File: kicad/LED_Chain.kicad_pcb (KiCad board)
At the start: 2 copper layers, 63.6 x 31.5 mm, 34 parts, among them J1 Interface, J2 PWR, J3 NeoPixel R1 A, J4 NeoPixel R1 B, J5 NeoPixel R1 C, J6 NeoPixel R1 D, J7 LED, Q1 IRLML2502, Q2 IRLML2502, Q3 IRLML2502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

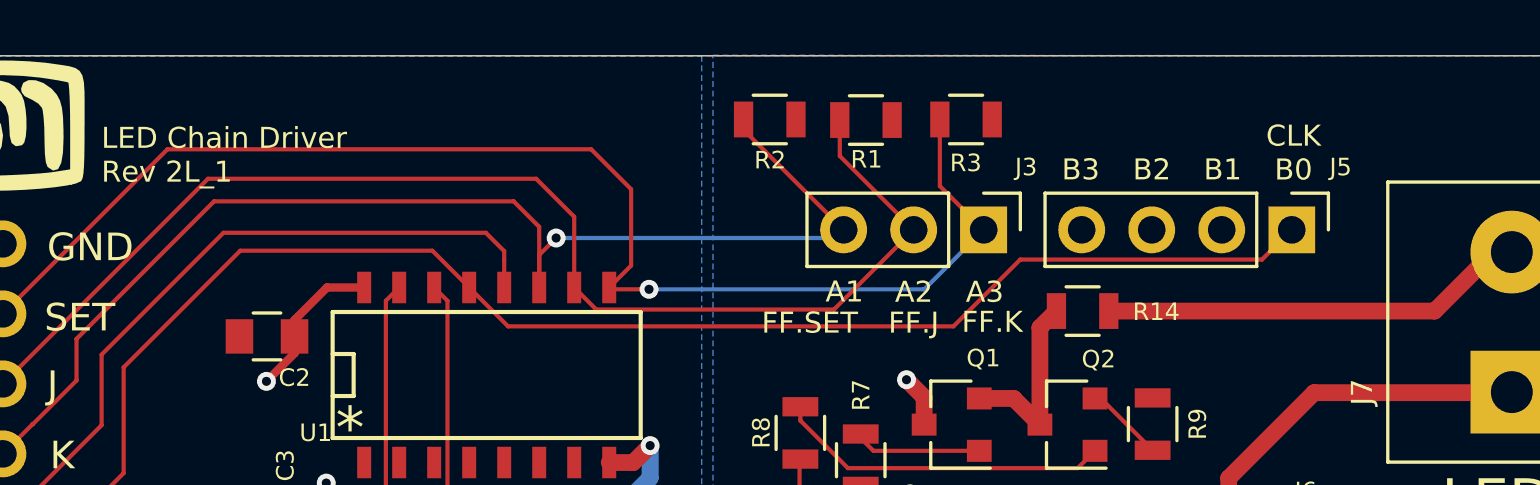
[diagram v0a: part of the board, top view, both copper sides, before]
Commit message: Revert "Fixes the pin association on J3"
This reverts commit 2cc36517f423e818af2cf15adf9433c164440afc.
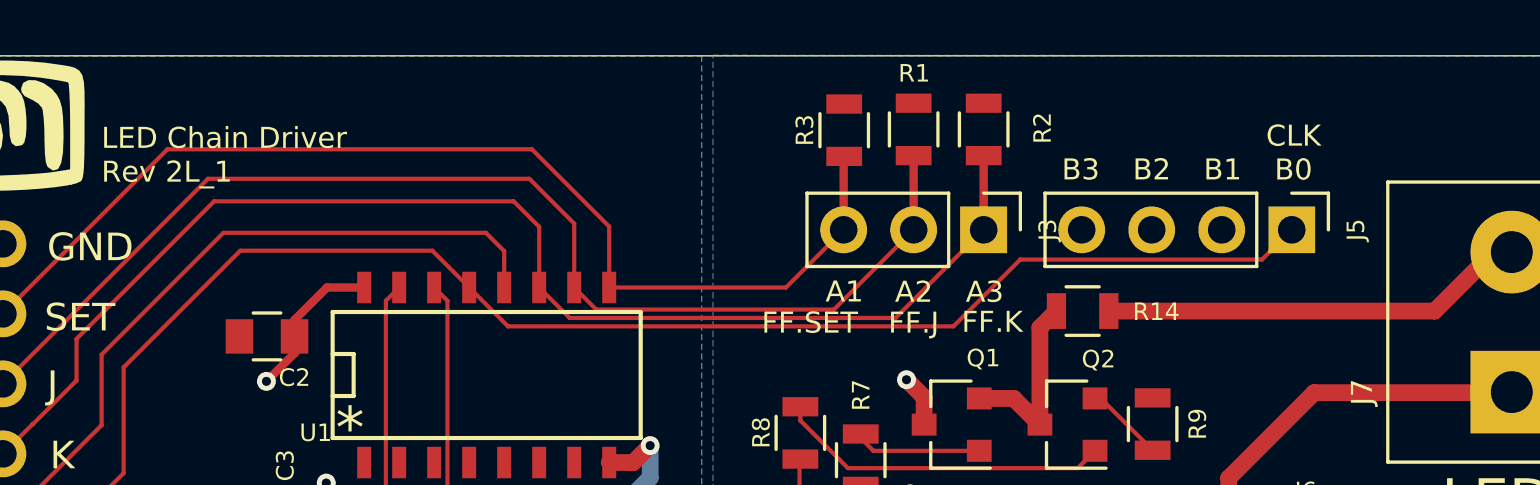
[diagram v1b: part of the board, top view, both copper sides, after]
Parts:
- moved R2 7.77 mm to (156.2, 82.6), turned to 90 degrees
- moved R3 4.44 mm to (151.2, 82.6), turned to 90 degrees
- moved R1 1.76 mm to (153.7, 82.6), turned to 90 degrees
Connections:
- J3 pad 1: /A1 -> /A3
- J3 pad 3: /A3 -> /A1
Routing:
- net /A1: track 49.0 -> 39.9 mm, vias 1 -> 0
- net /A2: track 45.9 -> 43.3 mm
- net /A3: track 44.8 -> 47.3 mm, vias 1 -> 0

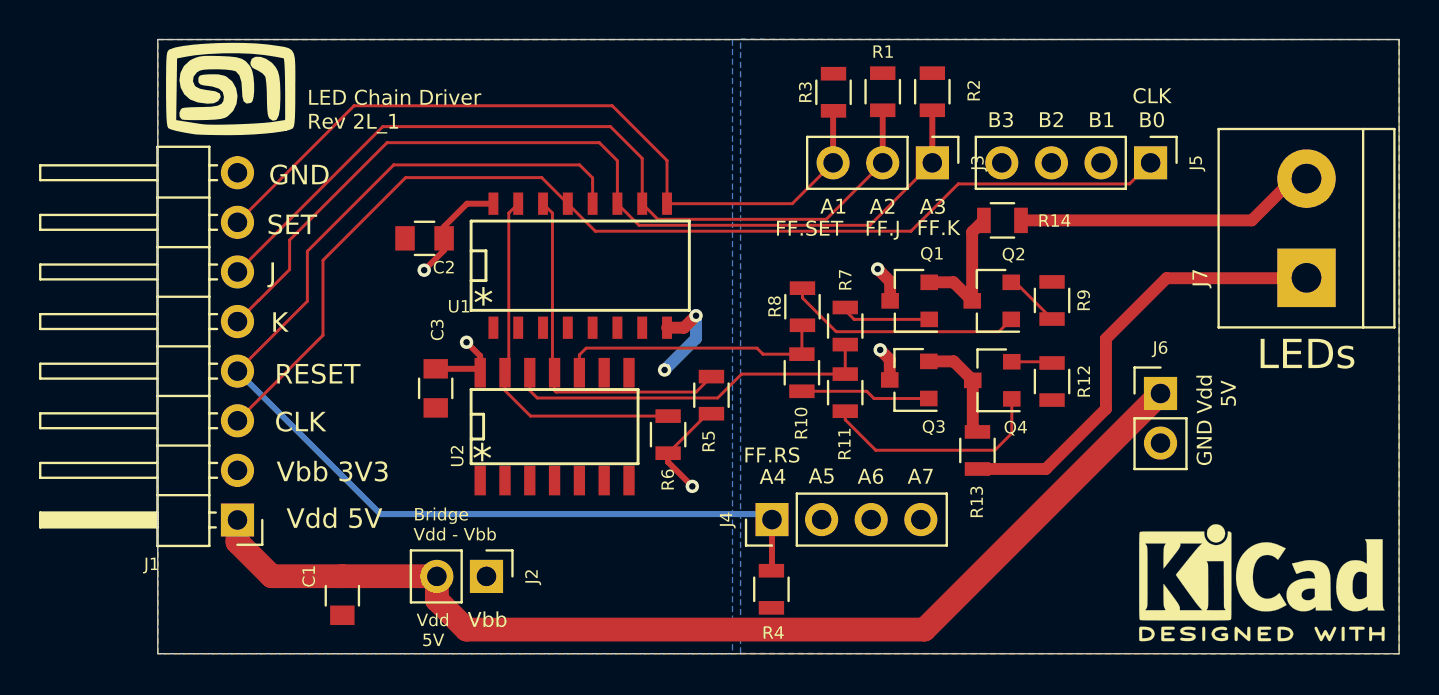
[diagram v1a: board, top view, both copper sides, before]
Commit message: Upgraded basic symbols and footprints
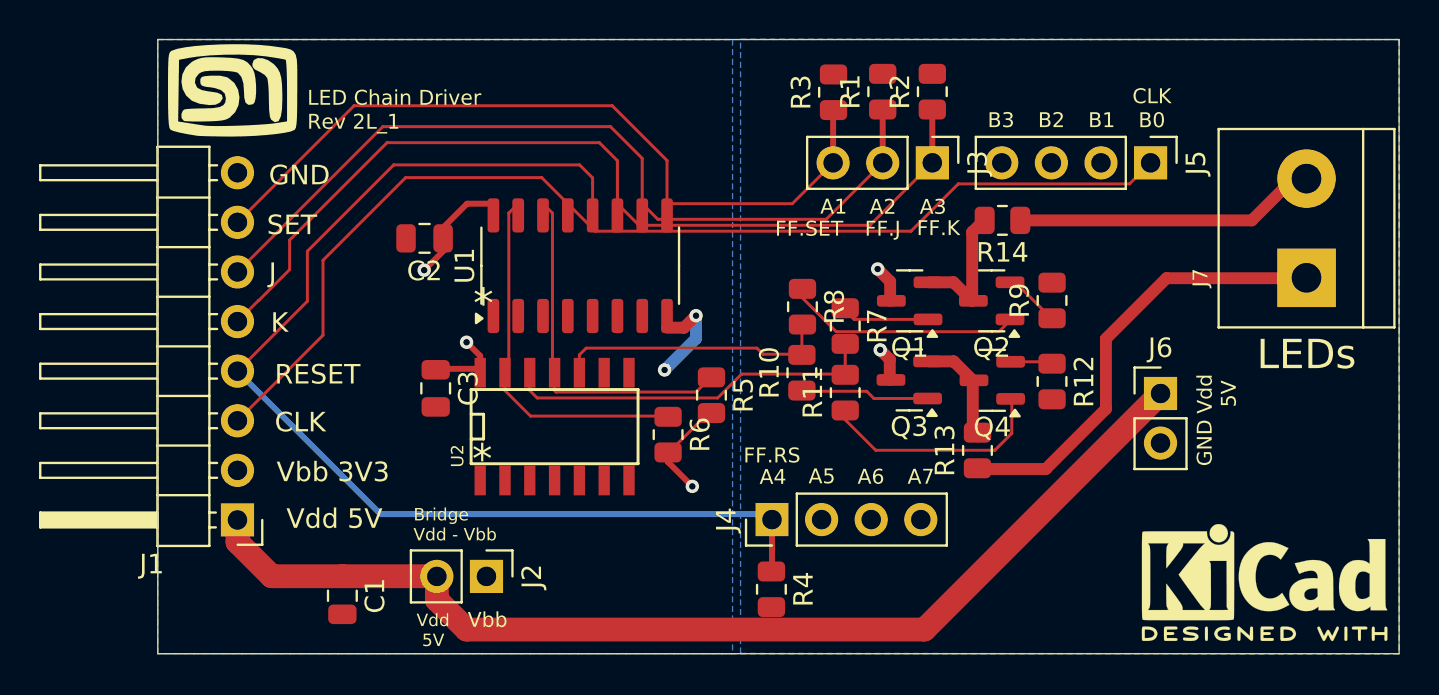
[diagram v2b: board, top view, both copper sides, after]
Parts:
- removed G*** (x2): LOGO, LED_Chain:MyBasic_rounded_50_1
- removed REF*** (x2): KiCad-Logo2_6mm_SilkScreen, Symbols:KiCad-Logo2_6mm_SilkScreen
- added Lg1: SM Logo, sjm-mechanical:MyBasic_rounded_50_1, F.Cu at (120.3, 82.5)
- added Lg2: KiCad Logo, Symbol:KiCad-Logo2_5mm_SilkScreen, F.Cu at (173.2, 107.7)
- added Lg3: SM Logo, sjm-mechanical:MyBasic_rounded_50_1, B.Cu at (149.7, 94.6)
- C1, C2, C3: footprint Capacitors_SMD:C_0805 -> Capacitor_SMD:C_0805_2012Metric
- J1: footprint Pin_Headers:Pin_Header_Angled_1x08_Pitch2.54mm -> Connector_PinHeader_2.54mm:PinHeader_1x08_P2.54mm_Horizontal
- J2, J6: footprint Pin_Headers:Pin_Header_Straight_1x02_Pitch2.54mm -> Connector_PinHeader_2.54mm:PinHeader_1x02_P2.54mm_Vertical
- J3: footprint Pin_Headers:Pin_Header_Straight_1x03_Pitch2.54mm -> Connector_PinHeader_2.54mm:PinHeader_1x03_P2.54mm_Vertical
- J4, J5: footprint Pin_Headers:Pin_Header_Straight_1x04_Pitch2.54mm -> Connector_PinHeader_2.54mm:PinHeader_1x04_P2.54mm_Vertical
- Q1, Q2, Q3, Q4: footprint TO_SOT_Packages_SMD:SOT-23 -> Package_TO_SOT_SMD:SOT-23
- R1, R10, R11, R12, R13, R14, R2, R3, R4, R5, R6, R7, R8, R9: footprint Resistors_SMD:R_0805 -> Resistor_SMD:R_0805_2012Metric
- U1: footprint SMD_Packages:SO-16-N -> Package_SO:SO-16_3.9x9.9mm_P1.27mm
- turned U1 to 90 degrees
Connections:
- net /~Q renamed /~{Q}
- J4 pad 2: (no net) -> /A5
- J4 pad 3: (no net) -> /A6
- J4 pad 4: (no net) -> /A7
- J5 pad 2: (no net) -> /B1
- J5 pad 3: (no net) -> /B2
- J5 pad 4: (no net) -> /B3
- U1 pad 1: (no net) -> unconnected-(U1A-Q-Pad1)
- U1 pad 2: (no net) -> unconnected-(U1A-~{Q}-Pad2)
- U1 pad 3: (no net) -> unconnected-(U1A-C-Pad3)
- U1 pad 4: (no net) -> unconnected-(U1A-R-Pad4)
- U1 pad 5: (no net) -> unconnected-(U1A-K-Pad5)
- U1 pad 6: (no net) -> unconnected-(U1A-J-Pad6)
- U1 pad 7: (no net) -> unconnected-(U1A-S-Pad7)
- U2 pad 1: (no net) -> unconnected-(U2-Pad1)
- U2 pad 2: (no net) -> unconnected-(U2-Pad2)
- U2 pad 3: (no net) -> unconnected-(U2-Pad3)
- U2 pad 4: (no net) -> unconnected-(U2-Pad4)
- U2 pad 5: (no net) -> unconnected-(U2-Pad5)
- U2 pad 6: (no net) -> unconnected-(U2-Pad6)
- U2 pad 8: (no net) -> unconnected-(U2-Pad8)
- U2 pad 9: (no net) -> unconnected-(U2-Pad9)
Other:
- net class Default removed

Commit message: Updated for V8 KiCad
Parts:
- U1: footprint Package_SO:SO-16_3.9x9.9mm_P1.27mm -> LED_Chain:SO-16-N
- turned U1 to 0 degrees
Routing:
- net Net-(Q2-S): track 2.87 -> 5.78 mm
- net /LED1: track 23.5 -> 20.9 mm
- net /L2: track 6.96 -> 8.73 mm
- net /5V: track 59.6 -> 58.7 mm
